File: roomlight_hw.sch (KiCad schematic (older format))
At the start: 35 parts

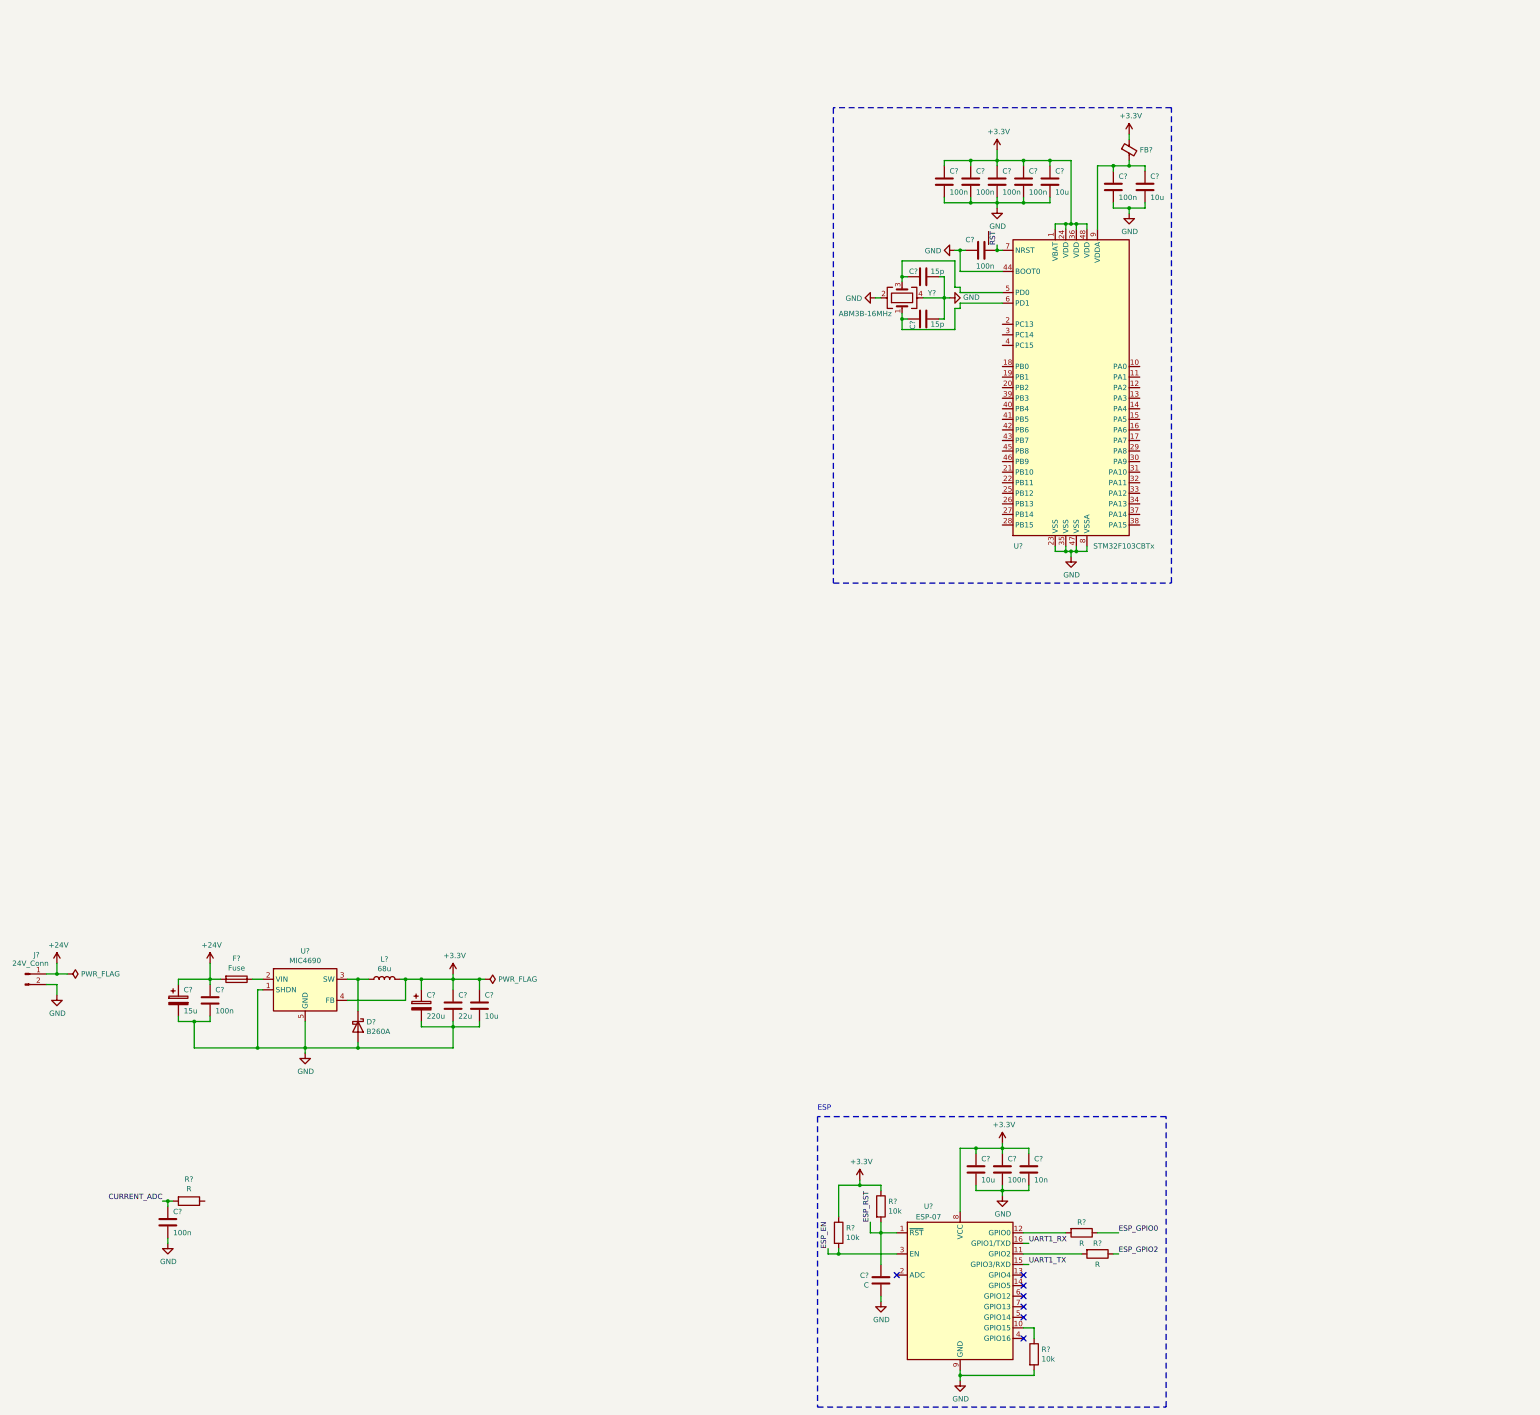
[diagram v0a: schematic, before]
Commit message: Finish schematic
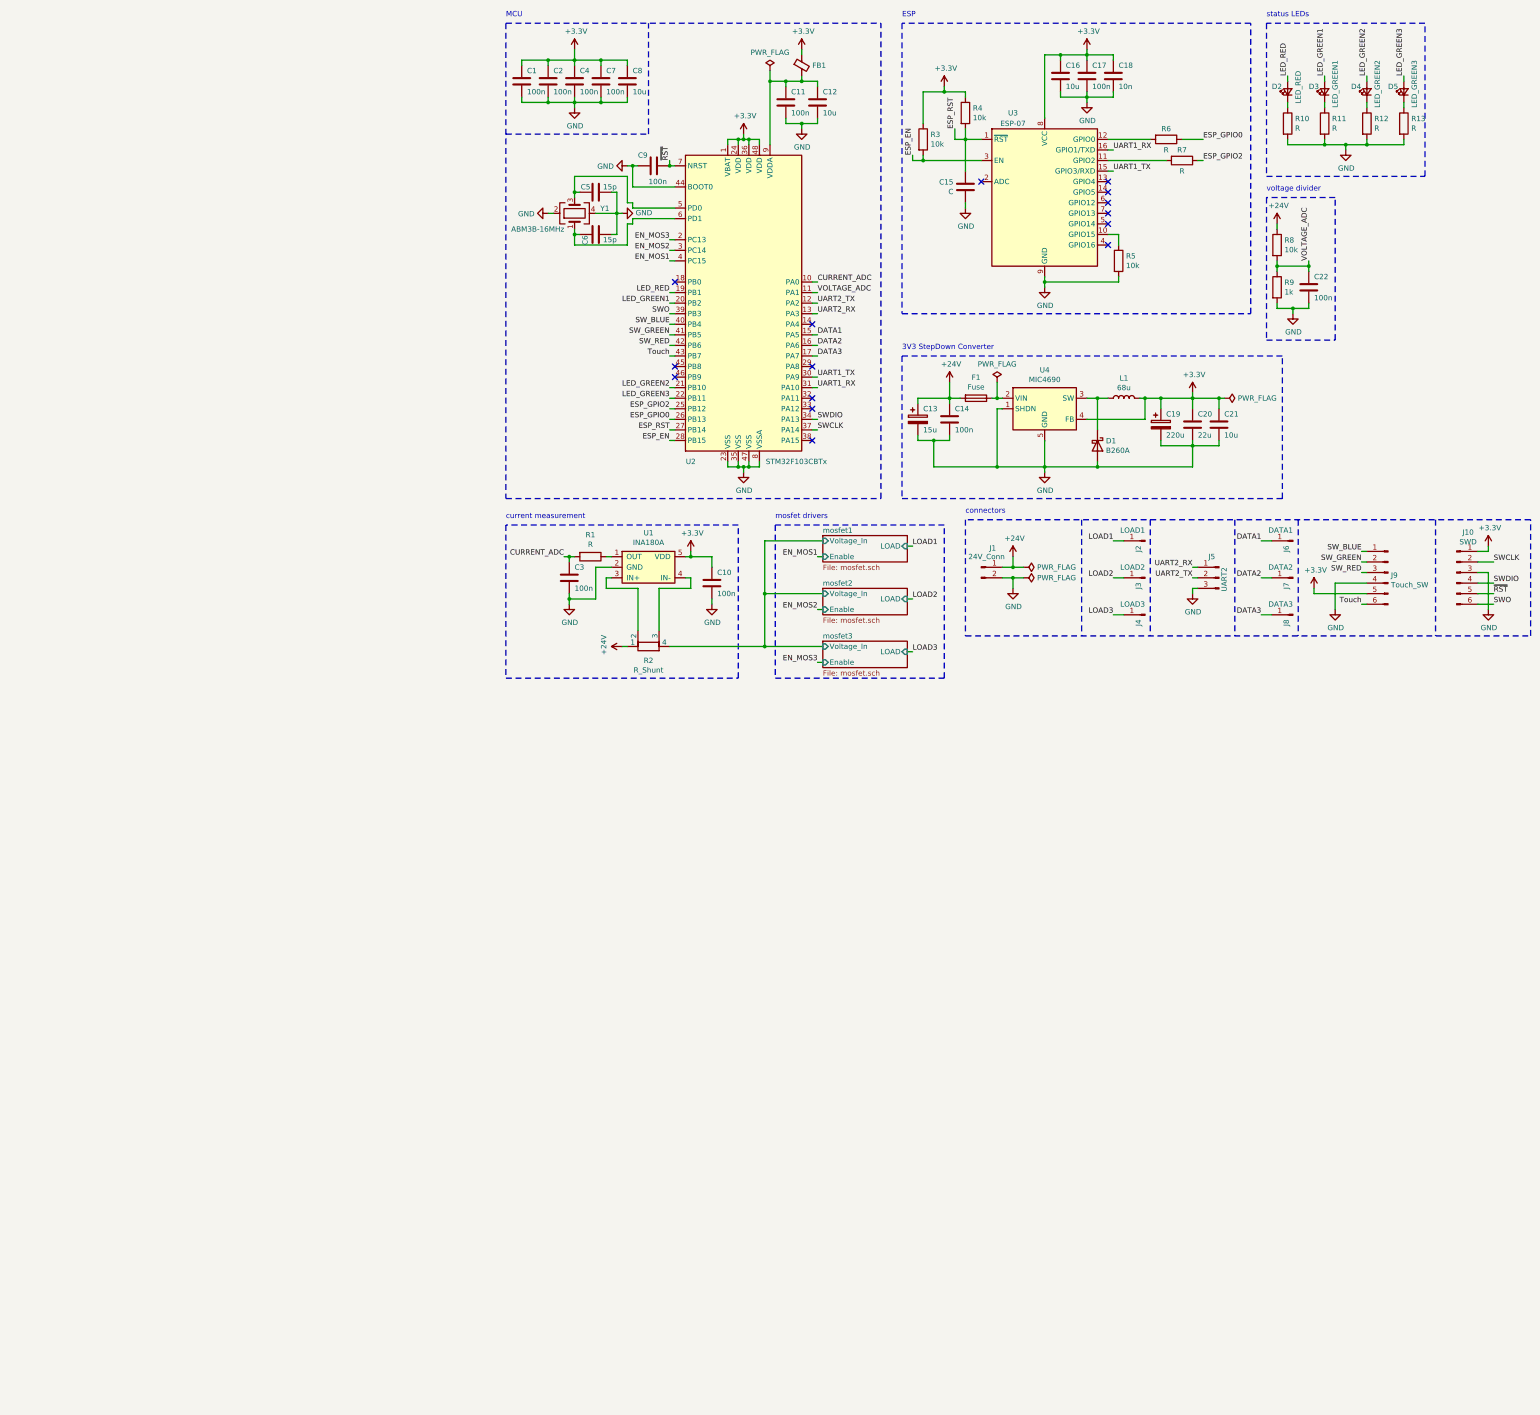
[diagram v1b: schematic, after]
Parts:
- added C10, C22: 100n, symbol Device:C
- added D2: LED_RED, symbol Device:LED_Small
- added D3: LED_GREEN1, symbol Device:LED_Small
- added D4: LED_GREEN2, symbol Device:LED_Small
- added D5: LED_GREEN3, symbol Device:LED_Small
- added J10: SWD, symbol Connector:Conn_01x06_Male
- added J2: LOAD1, symbol Connector:Conn_01x01_Male
- added J3: LOAD2, symbol Connector:Conn_01x01_Male
- added J4: LOAD3, symbol Connector:Conn_01x01_Male
- added J5: UART2, symbol Connector:Conn_01x03_Male
- added J6: DATA1, symbol Connector:Conn_01x01_Male
- added J7: DATA2, symbol Connector:Conn_01x01_Male
- added J8: DATA3, symbol Connector:Conn_01x01_Male
- added J9: Touch_SW, symbol Connector:Conn_01x06_Male
- added R10, R11, R12, R13: R, symbol Device:R
- added R2: R_Shunt, symbol Device:R_Shunt
- added R8: 10k, symbol Device:R
- added R9: 1k, symbol Device:R
- added U1: INA180A, symbol extra_symbols:INA180A
- gave numbers to parts that had none: 35
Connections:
- net +24V: now also R2.1, R8.1
- net +3V3: now also C10.2, J10.1 (Pin_1), J9.5 (Pin_5), U1.5 (VDD)
- net CURRENT_ADC: now also U2.10 (PA0)
- net ESP_EN: now also U2.28 (PB15)
- net ESP_GPIO0: now also U2.26 (PB13)
- net ESP_GPIO2: now also U2.25 (PB12)
- net ESP_RST: now also U2.27 (PB14)
- net GND: now also C10.1, C22.2, J10.3 (Pin_3), J5.3 (Pin_3), J9.4 (Pin_4), R10.2, R11.2, R12.2, R13.2, R9.2, U1.2 (GND)
- net UART1_RX: now also U2.31 (PA10)
- net UART1_TX: now also U2.30 (PA9)
- net ~RST: now also J10.5 (Pin_5)
- net VOLTAGE_ADC: now reaches U2.11 (PA1)
- net VOLTAGE_ADC: now also C22.1, R8.2, R9.1
- net UART2_TX: now reaches U2.12 (PA2)
- net UART2_TX: now also J5.2 (Pin_2)
- net UART2_RX: now reaches U2.13 (PA3)
- net UART2_RX: now also J5.1 (Pin_1)
- net DATA1: now reaches U2.15 (PA5)
- net DATA1: now also J6.1 (Pin_1)
- net DATA2: now reaches U2.16 (PA6)
- net DATA2: now also J7.1 (Pin_1)
- net DATA3: now reaches U2.17 (PA7)
- net DATA3: now also J8.1 (Pin_1)
- net LED_RED: now reaches U2.19 (PB1)
- net LED_RED: now also D2.2 (A)
- net EN_MOS3: now reaches U2.2 (PC13)
- net LED_GREEN1: now reaches U2.20 (PB2)
- net LED_GREEN1: now also D3.2 (A)
- net LED_GREEN2: now reaches U2.21 (PB10)
- net LED_GREEN2: now also D4.2 (A)
- net LED_GREEN3: now reaches U2.22 (PB11)
- net LED_GREEN3: now also D5.2 (A)
- net EN_MOS2: now reaches U2.3 (PC14)
- net SWDIO: now reaches U2.34 (PA13)
- net SWDIO: now also J10.4 (Pin_4)
- net SWCLK: now reaches U2.37 (PA14)
- net SWCLK: now also J10.2 (Pin_2)
- net SWO: now reaches U2.39 (PB3)
- net SWO: now also J10.6 (Pin_6)
- net EN_MOS1: now reaches U2.4 (PC15)
- net SW_BLUE: now reaches U2.40 (PB4)
- net SW_BLUE: now also J9.1 (Pin_1)
- net SW_GREEN: now reaches U2.41 (PB5)
- net SW_GREEN: now also J9.2 (Pin_2)
- net SW_RED: now reaches U2.42 (PB6)
- net SW_RED: now also J9.3 (Pin_3)
- net Touch: now reaches U2.43 (PB7)
- net Touch: now also J9.6 (Pin_6)
- net at R1.1: now also U1.1 (OUT)
- new net: R2.2, U1.3 (IN+)
- new net: R2.3, U1.4 (IN-)
- new net: D2.1 (K), R10.1
- new net: D5.1 (K), R13.1
- new net: D3.1 (K), R11.1
- new net: D4.1 (K), R12.1
- new net LOAD1: J2.1 (Pin_1)
- new net LOAD2: J3.1 (Pin_1)
- new net LOAD3: J4.1 (Pin_1)
- new net mosfet1/Voltage_In: R2.4
- no-connect marks 7 -> 15
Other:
- note added: "3V3 StepDown Converter"
- note added: "MCU"
- note added: "connectors"
- note added: "current measurement"
- note added: "mosfet drivers"
- note added: "status LEDs"
- note added: "voltage divider"
- moved on the sheet: C1, C11, C12, C13, C14, C15, C16, C17, C18, C19, C2, C20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

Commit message: Assign footprints
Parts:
- removed J3: LOAD2, symbol Connector:Conn_01x01_Male
- removed J4: LOAD3, symbol Connector:Conn_01x01_Male
- removed J6: DATA1, symbol Connector:Conn_01x01_Male
- removed J7: DATA2, symbol Connector:Conn_01x01_Male
- removed J8: DATA3, symbol Connector:Conn_01x01_Male
- added J4: DATAs, Connector_Molex:Molex_PicoBlade_53047-0310_1x03_P1.25mm_Vertical, symbol Connector:Conn_01x03_Male
- C1, C10, C11, C14, C17, C18, C2, C22, C3, C4, C7, C9: footprint (none) -> Capacitor_SMD:C_0603_1608Metric_Pad1.05x0.95mm_HandSolder
- C12, C16, C21, C8: footprint (none) -> Capacitor_SMD:C_0805_2012Metric_Pad1.15x1.40mm_HandSolder
- C13: footprint (none) -> Capacitor_THT:CP_Radial_D5.0mm_P2.50mm
- C15: value C -> 100n; footprint (none) -> Capacitor_SMD:C_0603_1608Metric_Pad1.05x0.95mm_HandSolder
- C19: footprint (none) -> Capacitor_THT:CP_Radial_D6.3mm_P2.50mm
- C20: value 22u -> 10u; footprint (none) -> Capacitor_SMD:C_0805_2012Metric_Pad1.15x1.40mm_HandSolder
- C5, C6: footprint (none) -> Capacitor_SMD:C_0402_1005Metric
- D1: footprint (none) -> Diode_SMD:D_SMB
- D2, D3, D4, D5: footprint (none) -> LED_SMD:LED_0805_2012Metric_Pad1.15x1.40mm_HandSolder
- F1: footprint (none) -> Fuse:Fuse_0603_1608Metric_Pad1.05x0.95mm_HandSolder
- FB1: footprint (none) -> Inductor_SMD:L_0805_2012Metric_Pad1.15x1.40mm_HandSolder
- J1: footprint (none) -> extraFootprints:DG306-5.08-02
- J2: value LOAD1 -> LOADs; footprint (none) -> extraFootprints:DG306-5.0-03; symbol Connector:Conn_01x01_Male -> Connector:Conn_01x03_Male
- J3: renamed from J5; footprint (none) -> Connector_Molex:Molex_PicoBlade_53047-0310_1x03_P1.25mm_Vertical
- J5: renamed from J9; footprint (none) -> Connector_Molex:Molex_PicoBlade_53047-0610_1x06_P1.25mm_Vertical
- J6: renamed from J10; footprint (none) -> Connector_PinHeader_2.54mm:PinHeader_1x06_P2.54mm_Vertical
- L1: footprint (none) -> Inductor_SMD:L_Taiyo-Yuden_NR-60xx
- R1, R10, R11, R12, R13, R3, R4, R5, R6, R7, R8, R9: footprint (none) -> Resistor_SMD:R_0603_1608Metric_Pad1.05x0.95mm_HandSolder
- R2: footprint (none) -> extraFootprints:R_2512_6332Metric_KelvinShunt
- U1: footprint (none) -> Package_TO_SOT_SMD:SOT-23-5
- Y1: footprint (none) -> Crystal:Crystal_SMD_Abracon_ABM3B-4Pin_5.0x3.2mm
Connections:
- net DATA1: now also J4.1 (Pin_1)
- net DATA2: now also J4.2 (Pin_2)
- net DATA3: now also J4.3 (Pin_3)
- net LOAD2: now also J2.2 (Pin_2)
- net LOAD3: now also J2.3 (Pin_3)
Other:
- moved on the sheet: J3

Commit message: Fix wrong footprint
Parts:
- J1: footprint extraFootprints:DG306-5.08-02 -> extraFootprints:DG306-5.0-02
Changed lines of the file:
@@
 F 0 "J1" H 5258 6031 50  0000 C CNN
 F 1 "24V_Conn" H 5200 5950 50  0000 C CNN
-F 2 "extraFootprints:DG306-5.08-02" H 5150 5850 50  0001 C CNN
+F 2 "extraFootprints:DG306-5.0-02" H 5150 5850 50  0001 C CNN
 F 3 "~" H 5150 5850 50  0001 C CNN
 	1    5150 5850

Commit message: Finish PCB
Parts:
- added H1, H2: MountingHole, MountingHole:MountingHole_3.2mm_M3_ISO14580, symbol Mechanical:MountingHole
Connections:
- net CURRENT_ADC: now also U2.11 (PA1); no longer U2.10 (PA0)
- net DATA1: now also U2.43 (PB7); no longer U2.15 (PA5)
- net DATA2: now also U2.45 (PB8); no longer U2.16 (PA6)
- net DATA3: now also U2.46 (PB9); no longer U2.17 (PA7)
- net ESP_EN: now also U2.22 (PB11); no longer U2.28 (PB15)
- net ESP_GPIO0: now also U2.20 (PB2); no longer U2.26 (PB13)
- net ESP_GPIO2: now also U2.19 (PB1); no longer U2.25 (PB12)
- net ESP_RST: now also U2.21 (PB10); no longer U2.27 (PB14)
- net LED_GREEN1: now also U2.15 (PA5); no longer U2.20 (PB2)
- net LED_GREEN2: now also U2.16 (PA6); no longer U2.21 (PB10)
- net LED_GREEN3: now also U2.17 (PA7); no longer U2.22 (PB11)
- net LED_RED: now also U2.14 (PA4); no longer U2.19 (PB1)
- net LOAD1: now also J2.3 (Pin_3); no longer J2.1 (Pin_1)
- net LOAD3: now also J2.1 (Pin_1); no longer J2.3 (Pin_3)
- net SW_BLUE: now also U2.38 (PA15); no longer U2.40 (PB4)
- net SW_GREEN: now also U2.40 (PB4); no longer U2.41 (PB5)
- net SW_RED: now also U2.41 (PB5); no longer U2.42 (PB6)
- net Touch: now also U2.42 (PB6); no longer U2.43 (PB7)
- net UART1_RX: now also J3.2 (Pin_2); no longer U3.16 (GPIO1/TXD)
- net UART1_TX: now also J3.1 (Pin_1); no longer U3.15 (GPIO3/RXD)
- net UART2_RX: now also U3.16 (GPIO1/TXD); no longer J3.1 (Pin_1)
- net UART2_TX: now also U3.15 (GPIO3/RXD); no longer J3.2 (Pin_2)
- net VOLTAGE_ADC: now also U2.10 (PA0); no longer U2.11 (PA1)
- net IN+: now reaches R2.2, U1.3 (IN+)
- net IN-: now reaches R2.3, U1.4 (IN-)
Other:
- note added: "PCB mounting holes"
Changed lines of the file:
@@
 Text Label 7250 2000 0    50   ~ 0
 ESP_GPIO2
-Text Label 6400 1900 0    50   ~ 0
+Text Label 7200 5950 2    50   ~ 0
 UART1_RX
 Wire Wire Line
 	6400 1900 6350 1900
-Text Label 6400 2100 0    50   ~ 0
+Text Label 7200 5850 2    50   ~ 0
 UART1_TX
 Wire Wire Line
@@
 F0 "mosfet1" 50
 F1 "mosfet.sch" 50
-F2 "LOAD" I R 4450 5650 50
-F3 "Enable" I L 3650 5750 50
-F4 "Voltage_In" I L 3650 5600 50
+F2 "Enable" I L 3650 5750 50
+F3 "Voltage_In" I L 3650 5600 50
+F4 "LOAD" O R 4450 5650 50
 $EndSheet
 Wire Notes Line
@@
 F0 "mosfet2" 50
 F1 "mosfet.sch" 50
-F2 "LOAD" I R 4450 6150 50
-F3 "Enable" I L 3650 6250 50
-F4 "Voltage_In" I L 3650 6100 50
+F2 "Enable" I L 3650 6250 50
+F3 "Voltage_In" I L 3650 6100 50
+F4 "LOAD" O R 4450 6150 50
 $EndSheet
 $Sheet
@@
 F0 "mosfet3" 50
 F1 "mosfet.sch" 50
-F2 "LOAD" I R 4450 6650 50
-F3 "Enable" I L 3650 6750 50
-F4 "Voltage_In" I L 3650 6600 50
+F2 "Enable" I L 3650 6750 50
+F3 "Voltage_In" I L 3650 6600 50
+F4 "LOAD" O R 4450 6650 50
 $EndSheet
 Wire Wire Line
@@
 Text Notes 7850 2300 0    50   ~ 0
 voltage divider
+Text Label 3600 3250 0    50   ~ 0
+CURRENT_ADC
 Text Label 3600 3150 0    50   ~ 0
-CURRENT_ADC
-Text Label 3600 3250 0    50   ~ 0
 VOLTAGE_ADC
 Wire Wire Line
@@
 Wire Wire Line
 	3550 4150 3600 4150
-Text Label 2200 4550 2    50   ~ 0
+Text Label 2200 4150 2    50   ~ 0
 ESP_RST
-Text Label 2200 4650 2    50   ~ 0
+Text Label 2200 4250 2    50   ~ 0
 ESP_EN
 Text Label 2200 2950 2    50   ~ 0
@@
 Wire Wire Line
 	2200 2950 2250 2950
-Text Label 2200 4450 2    50   ~ 0
+Text Label 2200 3350 2    50   ~ 0
 ESP_GPIO0
-Text Label 2200 4350 2    50   ~ 0
+Text Label 2200 3250 2    50   ~ 0
 ESP_GPIO2
-Text Label 2200 4250 2    50   ~ 0
+Text Label 3600 3850 0    50   ~ 0
 LED_GREEN3
-Text Label 2200 3250 2    50   ~ 0
+Text Label 3600 3550 0    50   ~ 0
 LED_RED
-Text Label 2200 3350 2    50   ~ 0
+Text Label 3600 3650 0    50   ~ 0
 LED_GREEN1
-Text Label 2200 4150 2    50   ~ 0
+Text Label 3600 3750 0    50   ~ 0
 LED_GREEN2
-Wire Wire Line
-	2200 4650 2250 4650
-Wire Wire Line
-	2250 4550 2200 4550
-Wire Wire Line
-	2200 4450 2250 4450
-Wire Wire Line
-	2250 4350 2200 4350
-Wire Wire Line
-	2200 3250 2250 3250
-Wire Wire Line
-	2250 3350 2200 3350
-Wire Wire Line
-	2200 4250 2250 4250
-Wire Wire Line
-	2250 4150 2200 4150
-Text Label 2200 3850 2    50   ~ 0
+Text Label 2200 3750 2    50   ~ 0
 Touch
-Text Label 2200 3750 2    50   ~ 0
+Text Label 2200 3650 2    50   ~ 0
 SW_RED
-Text Label 2200 3650 2    50   ~ 0
+Text Label 2200 3550 2    50   ~ 0
 SW_GREEN
-Text Label 2200 3550 2    50   ~ 0
+Text Label 3600 4650 0    50   ~ 0
 SW_BLUE
 Wire Wire Line
@@
 F 3 "~" H 6700 5950 50  0001 C CNN
 	1    6700 5950
-	-1   0    0    -1
+	-1   0    0    1
 $EndComp
 Text Label 6400 5850 2    50   ~ 0
@@
 Text Label 3600 3450 0    50   ~ 0
 UART2_RX
-Text Label 7200 5850 2    50   ~ 0
+Text Label 6400 1900 0    50   ~ 0
 UART2_RX
-Text Label 7200 5950 2    50   ~ 0
+Text Label 6400 2100 0    50   ~ 0
 UART2_TX
-Text Label 3600 3650 0    50   ~ 0
+Text Label 2200 3850 2    50   ~ 0
 DATA1
-Text Label 3600 3750 0    50   ~ 0
+Text Label 2200 3950 2    50   ~ 0
 DATA2
-Text Label 3600 3850 0    50   ~ 0
+Text Label 2200 4050 2    50   ~ 0
 DATA3
 Wire Wire Line
@@
 Wire Wire Line
 	3600 3650 3550 3650
-NoConn ~ 3550 3550
 NoConn ~ 3550 3950
 NoConn ~ 3550 4250
 NoConn ~ 3550 4350
-NoConn ~ 3550 4650
-NoConn ~ 2250 3950
-NoConn ~ 2250 4050
 NoConn ~ 2250 3150
 $Comp
@@
 Text Label 8750 6200 2    50   ~ 0
 Touch
+$Comp
+L Mechanical:MountingHole H1
+U 1 1 5F33C7CD
+P 9550 800
+F 0 "H1" H 9650 846 50  0000 L CNN
+F 1 "MountingHole" H 9650 755 50  0000 L CNN
+F 2 "MountingHole:MountingHole_3.2mm_M3_ISO14580" H 9550 800 50  0001 C CNN
+F 3 "~" H 9550 800 50  0001 C CNN
+	1    9550 800
+	1    0    0    -1
+$EndComp
+$Comp
+L Mechanical:MountingHole H2
+U 1 1 5F33CA20
+P 9550 1050
+F 0 "H2" H 9650 1096 50  0000 L CNN
+F 1 "MountingHole" H 9650 1005 50  0000 L CNN
+F 2 "MountingHole:MountingHole_3.2mm_M3_ISO14580" H 9550 1050 50  0001 C CNN
+F 3 "~" H 9550 1050 50  0001 C CNN
+	1    9550 1050
+	1    0    0    -1
+$EndComp
+Wire Notes Line
+	9450 700  9450 1200
+Wire Notes Line
+	9450 1200 10200 1200
+Wire Notes Line
+	10200 1200 10200 700
+Wire Notes Line
+	10200 700  9450 700
+Text Notes 9450 650  0    50   ~ 0
+PCB mounting holes
+Text Label 1900 6150 3    50   ~ 0
+IN+
+Text Label 2100 6150 3    50   ~ 0
+IN-
+Wire Wire Line
+	3600 4650 3550 4650
+Wire Wire Line
+	2250 4050 2200 4050
+Wire Wire Line
+	2250 3950 2200 3950
+Wire Wire Line
+	3600 3550 3550 3550
+Wire Wire Line
+	2250 4150 2200 4150
+Wire Wire Line
+	2200 4250 2250 4250
+Wire Wire Line
+	2200 3350 2250 3350
+Wire Wire Line
+	2250 3250 2200 3250
+NoConn ~ 2250 4350
+NoConn ~ 2250 4450
+NoConn ~ 2250 4550
+NoConn ~ 2250 4650
+$Comp
+L power:PWR_FLAG #FLG0101
+U 1 1 5F31C560
+P 3100 5450
+F 0 "#FLG0101" H 3100 5525 50  0001 C CNN
+F 1 "PWR_FLAG" H 3100 5623 50  0000 C CNN
+F 2 "" H 3100 5450 50  0001 C CNN
+F 3 "~" H 3100 5450 50  0001 C CNN
+	1    3100 5450
+	1    0    0    -1
+$EndComp
+Wire Wire Line
+	3100 5450 3100 5600
+Connection ~ 3100 5600
 $EndSCHEMATC
